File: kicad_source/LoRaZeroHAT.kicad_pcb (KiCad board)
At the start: 2 copper layers, 65 x 30 mm, 35 parts, among them CN1 RASPI-IO, J1 BM04B-SRSS-TB, U1 24LC32, U2 NEO-M8N, U3 Ai-Thinker-Ra-01, U4 BME280

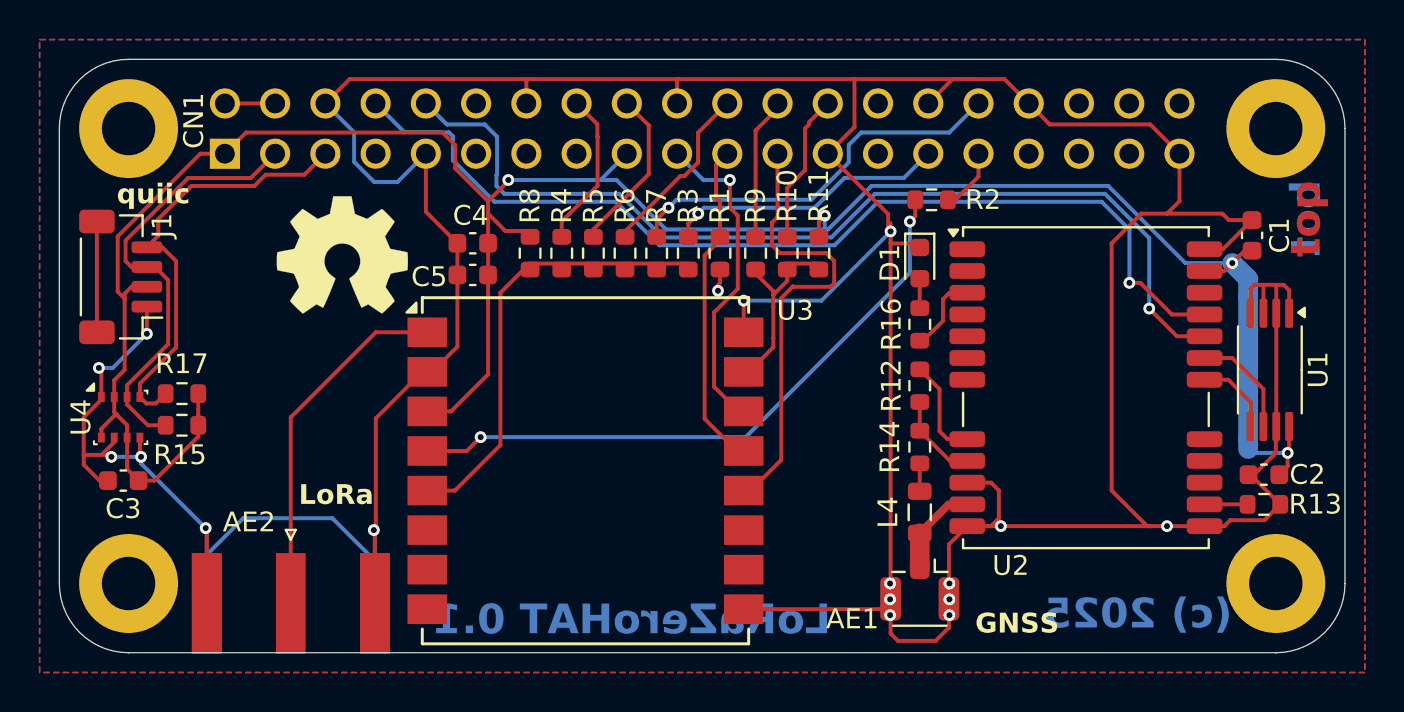
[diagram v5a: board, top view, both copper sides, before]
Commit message: updated layout
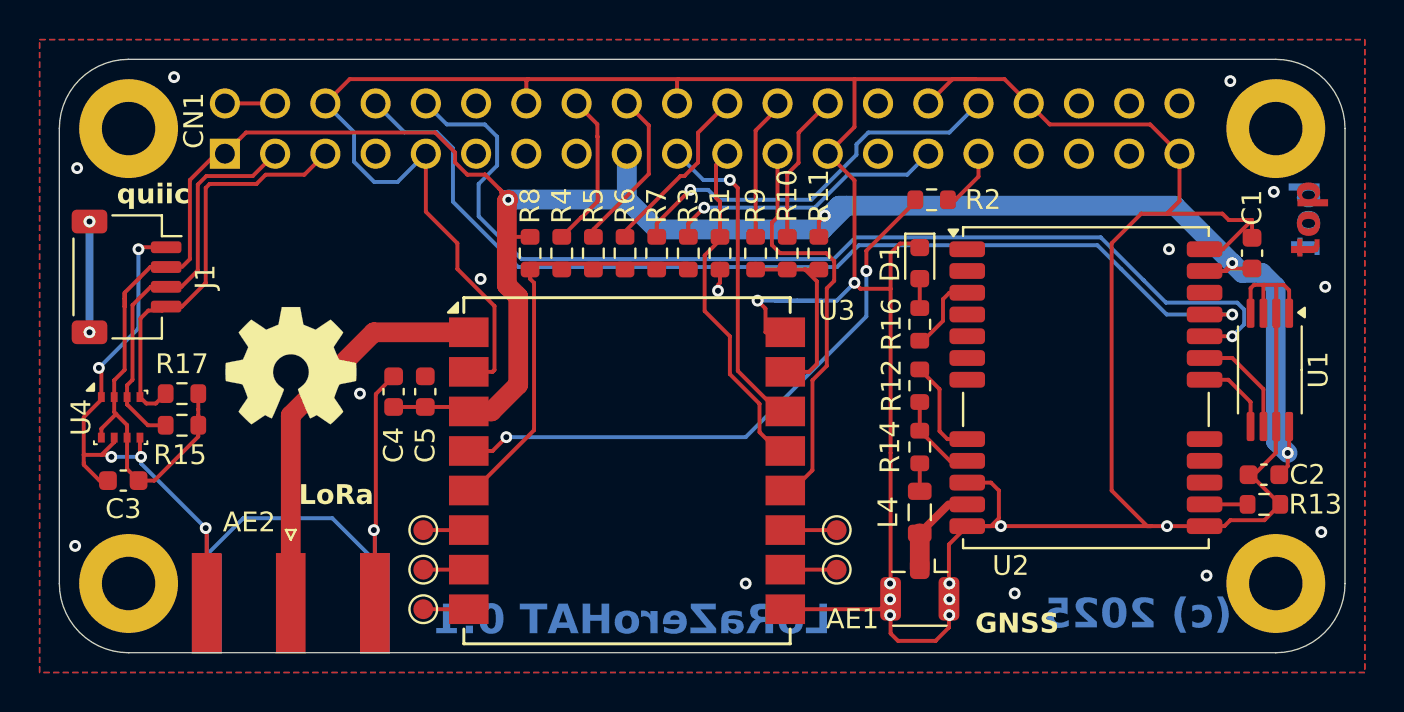
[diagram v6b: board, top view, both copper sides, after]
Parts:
- added TP1: TestPoint, TestPoint:TestPoint_Pad_D1.0mm, F.Cu at (121.4, 110.8)
- added TP2: TestPoint, TestPoint:TestPoint_Pad_D1.0mm, F.Cu at (121.4, 112.8)
- added TP3: TestPoint, TestPoint:TestPoint_Pad_D1.0mm, F.Cu at (121.4, 114.8)
- added TP4: TestPoint, TestPoint:TestPoint_Pad_D1.0mm, F.Cu at (142.3, 112.8)
- added TP5: TestPoint, TestPoint:TestPoint_Pad_D1.0mm, F.Cu at (142.3, 110.8)
- J1: value BM04B-SRSS-TB -> SM04B-SRSS-TB; footprint Connector_JST:JST_SH_BM04B-SRSS-TB_1x04-1MP_P1.00mm_Vertical -> Connector_JST:JST_SH_SM04B-SRSS-TB_1x04-1MP_P1.00mm_Horizontal
- moved C4 8.50 mm to (119.9, 103.8), turned to 90 degrees
- moved C5 6.37 mm to (121.5, 103.8), turned to 90 degrees
- moved L1 6.17 mm to (114.7, 102.5)
- moved L2 2.76 mm to (117.5, 99.7), turned to 0 degrees
- moved U3 2.10 mm to (131.7, 107.8)
- moved C1 0.90 mm to (163.3, 96.8)
- moved J1 0.30 mm to (106.4, 98.0), turned to -90 degrees
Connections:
- U3 pad 10: unconnected-(U3-DIO4-Pad10) -> /LoRa GNSS/LORA_DIO4
- U3 pad 11: unconnected-(U3-DIO5-Pad11) -> /LoRa GNSS/LORA_DIO5
- U3 pad 6: unconnected-(U3-DIO1-Pad6) -> /LoRa GNSS/LORA_DIO1
- U3 pad 7: unconnected-(U3-DIO2-Pad7) -> /LoRa GNSS/LORA_DIO2
- U3 pad 8: unconnected-(U3-DIO3-Pad8) -> /LoRa GNSS/LORA_DIO3
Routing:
- net GND: track 260.9 -> 266.7 mm, vias 17 -> 30
- net SERIAL_RX: track 49.7 -> 53.3 mm
- net +3.3V: track 124.7 -> 127.3 mm
- net /LoRa GNSS/LORA_DIO5: track 0.00 -> 2.60 mm
- net /LoRa GNSS/LORA_DIO4: track 0.00 -> 2.60 mm
- net /LoRa GNSS/LORA_DIO3: track 0.00 -> 2.30 mm
- net /LoRa GNSS/LORA_DIO2: track 0.00 -> 2.30 mm
- net /LoRa GNSS/LORA_DIO1: track 0.00 -> 2.30 mm
- net /LoRa GNSS/LORA_ANTENNA: track 18.1 -> 20.2 mm
- net LORA_RESET: track 31.9 -> 29.8 mm
- net I2C_SDA: track 22.5 -> 20.4 mm
- net SPI_SCK: track 23.1 -> 21.1 mm
- net LORA_INT: track 22.5 -> 20.8 mm
- net I2C_SCL: track 22.5 -> 21.2 mm
- net SERIAL_TX: track 50.4 -> 51.6 mm
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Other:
- board text added: "for Ai-Thinker Ra-01 and compatible"

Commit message: updated label
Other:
- board text added: "licensed under CERN-OHL-W v2"
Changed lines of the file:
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@@
 		(at 117.48095 99.73645)
 		(property "Reference" "L2"
-			(at 0 0 360)
+			(at 0 0 0)
 			(layer "F.SilkS")
 			(hide yes)
@@
 		)
 		(property "Value" "Label"
-			(at 0.75 0 360)
+			(at 0.75 0 0)
 			(layer "F.SilkS")
 			(hide yes)
@@
 		)
 		(property "Footprint" "generationmake:generationmake_small_solder"
-			(at 0 0 360)
+			(at 0 0 0)
 			(layer "F.Fab")
 			(hide yes)
@@
 		)
 		(property "Datasheet" ""
-			(at 0 0 360)
+			(at 0 0 0)
 			(layer "F.Fab")
 			(hide yes)
@@
 		)
 		(property "Description" ""
-			(at 0 0 360)
+			(at 0 0 0)
 			(layer "F.Fab")
 			(hide yes)
@@
 				(bold yes)
 			)
+			(justify left bottom mirror)
+		)
+	)
+	(gr_text "licensed under CERN-OHL-W v2"
+		(at 130.3 95.9 0)
+		(layer "B.SilkS")
+		(effects
+			(font
+				(size 1 1)
+				(thickness 0.25)
+				(bold yes)
+			)

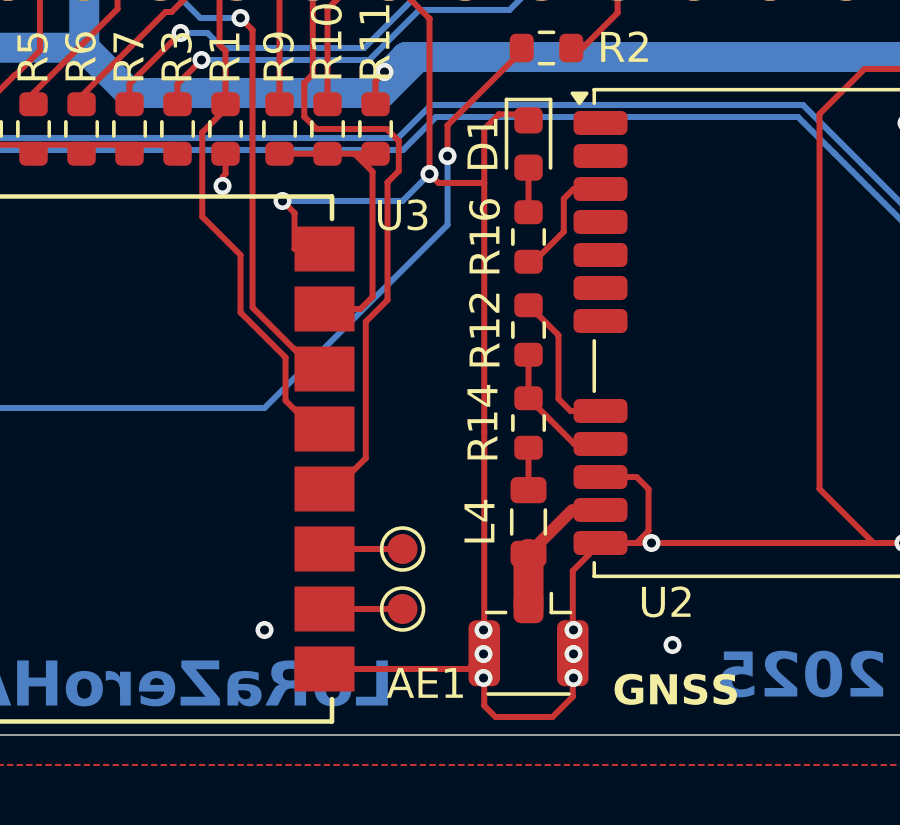
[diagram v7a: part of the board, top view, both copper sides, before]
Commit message: added capacitor C6 on u-blox VCC_RF
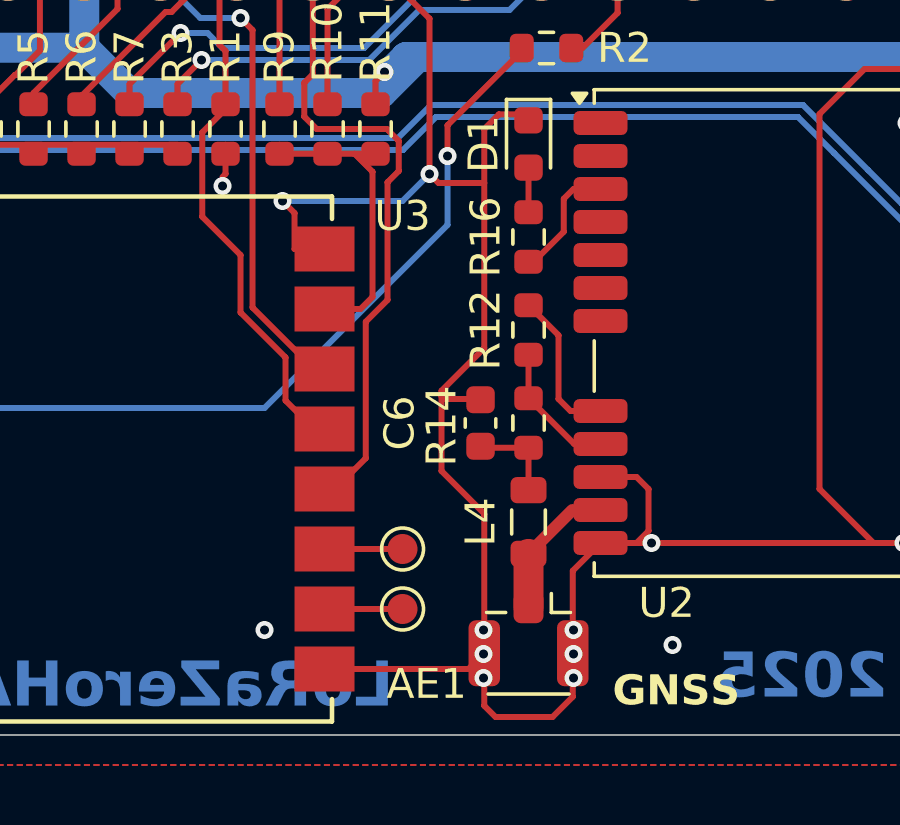
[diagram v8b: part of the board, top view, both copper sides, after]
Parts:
- added C6: 100 nF, Capacitor_SMD:C_0603_1608Metric, F.Cu at (144.9, 106.6)
- R14: value 1k -> 10R
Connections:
- J1 pad MP: unconnected-(J1-MountPin-PadMP) -> /LoRa GNSS/MP
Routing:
- net unconnected-(J1-MountPin-PadMP): track 5.60 -> 0.00 mm, vias 2 -> 0
- net (no net): track 0.00 -> 5.60 mm, vias 0 -> 2
- net GND: track 266.7 -> 269.2 mm
- net Net-(C6-Pad1): track 1.41 -> 3.03 mm
